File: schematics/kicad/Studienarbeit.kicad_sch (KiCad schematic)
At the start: 65 parts, among them J1 Barrel_Jack_Switch, U1 ESP32-WROOM-32E, U2 PCM5102, U3 MCP6001-OT, U4 MCP6001-OT, U5 MCP6001, U6 TPA711, U7 LM2940CT-5.0

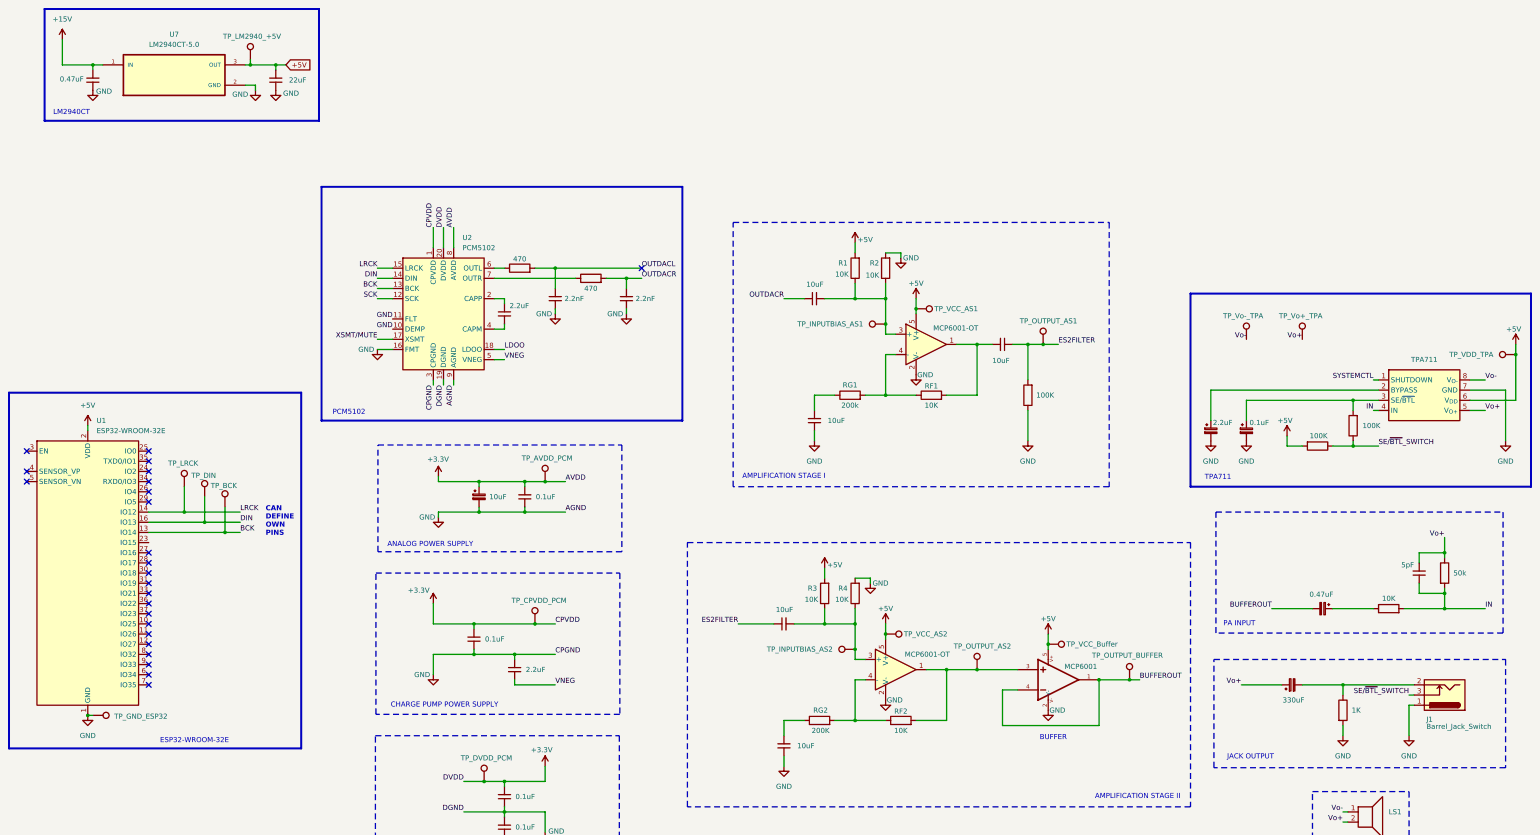
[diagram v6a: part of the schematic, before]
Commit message: Replace ESP32 Schematic with header pins.
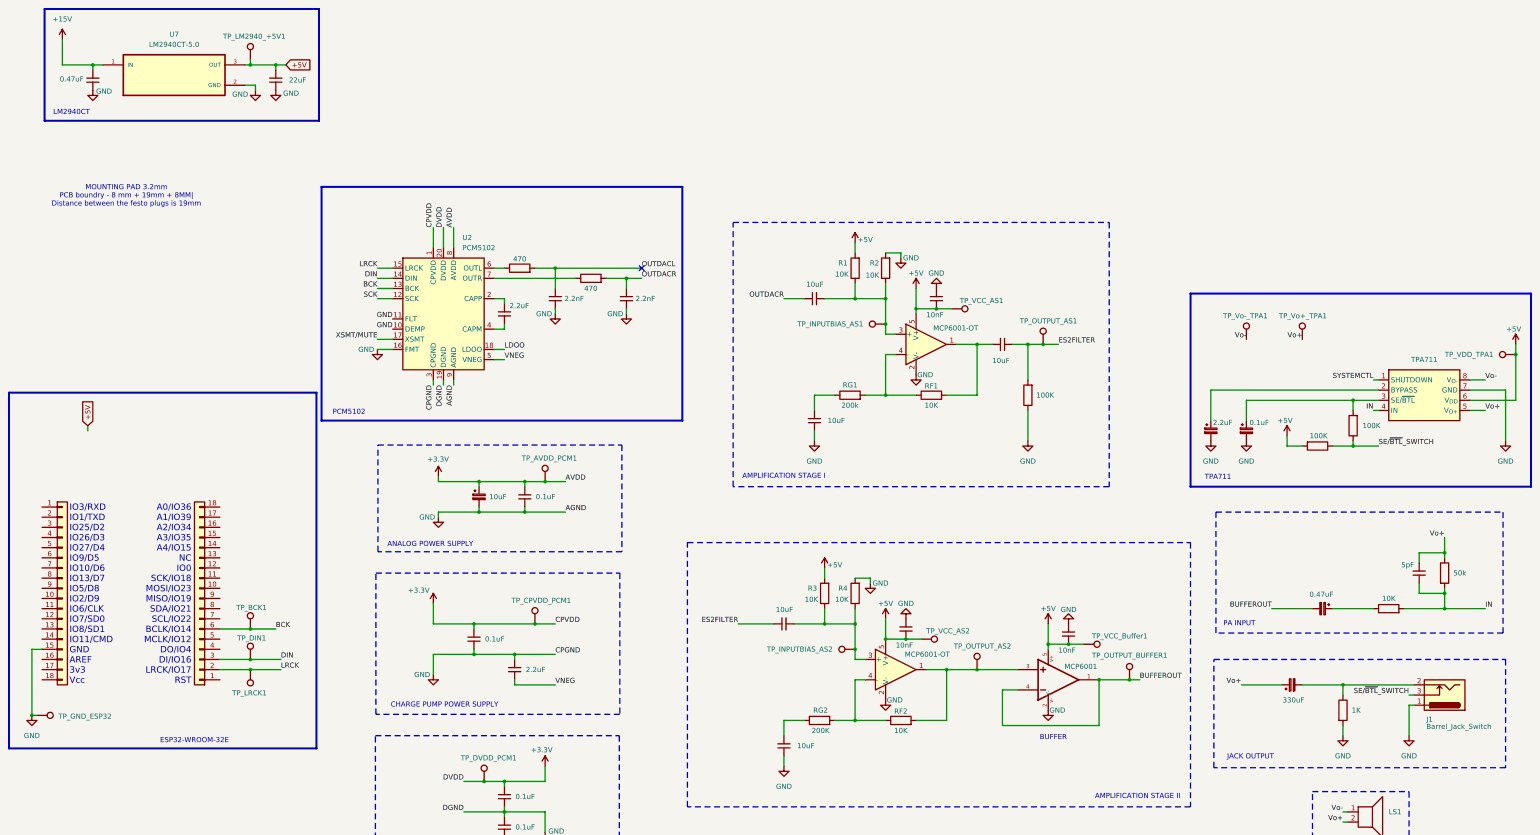
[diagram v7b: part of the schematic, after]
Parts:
- removed U1: ESP32-WROOM-32E, RF_Module:ESP32-WROOM-32E, symbol RF_Module:ESP32-WROOM-32E
- added C_COUPLING_AMPSTAGE2, C_COUPLING_AMPSTAGE3, C_COUPLING_AMPSTAGE4: 10nF, Capacitor_SMD:C_1206_3216Metric_Pad1.33x1.80mm_HandSolder, symbol Device:C_Small
- added J2, J3: Conn_01x18, Connector_PinSocket_2.54mm:PinSocket_1x18_P2.54mm_Vertical, symbol Connector_Generic:Conn_01x18
- TP_AVDD_PCM1: renamed from TP_AVDD_PCM; footprint (none) -> TestPoint:TestPoint_Pad_1.5x1.5mm
- TP_BCK1: renamed from TP_BCK; footprint (none) -> TestPoint:TestPoint_Pad_1.5x1.5mm
- TP_CPVDD_PCM1: renamed from TP_CPVDD_PCM; footprint (none) -> TestPoint:TestPoint_Pad_1.5x1.5mm
- TP_DIN1: renamed from TP_DIN; footprint (none) -> TestPoint:TestPoint_Pad_1.5x1.5mm
- TP_DVDD_PCM1: renamed from TP_DVDD_PCM; footprint (none) -> TestPoint:TestPoint_Pad_1.5x1.5mm
- TP_GND_ESP32, TP_INPUTBIAS_AS1, TP_INPUTBIAS_AS2, TP_OUTPUT_AS1, TP_OUTPUT_AS2, TP_VCC_AS1, TP_VCC_AS2: footprint (none) -> TestPoint:TestPoint_Pad_1.5x1.5mm
- TP_LM2940_+5V1: renamed from TP_LM2940_+5V; footprint (none) -> TestPoint:TestPoint_Pad_1.5x1.5mm
- TP_LRCK1: renamed from TP_LRCK; footprint (none) -> TestPoint:TestPoint_Pad_1.5x1.5mm
- TP_OUTPUT_BUFFER1: renamed from TP_OUTPUT_BUFFER; footprint (none) -> TestPoint:TestPoint_Pad_1.5x1.5mm
- TP_VCC_Buffer1: renamed from TP_VCC_Buffer; footprint (none) -> TestPoint:TestPoint_Pad_1.5x1.5mm
- TP_VDD_TPA1: renamed from TP_VDD_TPA; footprint (none) -> TestPoint:TestPoint_Pad_1.5x1.5mm
- TP_Vo+_TPA1: renamed from TP_Vo+_TPA; footprint (none) -> TestPoint:TestPoint_Pad_1.5x1.5mm
- TP_Vo-_TPA1: renamed from TP_Vo-_TPA; footprint (none) -> TestPoint:TestPoint_Pad_1.5x1.5mm
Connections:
- net +5V: now also C_COUPLING_AMPSTAGE2.2, C_COUPLING_AMPSTAGE3.2, C_COUPLING_AMPSTAGE4.2
- net BCK: now also J3.6 (Pin_6)
- net DIN: now also J3.3 (Pin_3)
- net GND: now also C_COUPLING_AMPSTAGE2.1, C_COUPLING_AMPSTAGE3.1, C_COUPLING_AMPSTAGE4.1, J2.15 (Pin_15)
- net LRCK: now also J3.2 (Pin_2)
- no-connect marks 24 -> 1
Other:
- note added: "A0/IO36 A1/IO39 A2/IO34 A3/IO35 A4/IO15 NC IO0 SCK/IO18 MOSI/IO23 MISO/IO19 SDA/IO21 SCL/IO22 BCLK/IO14 MCLK/IO12 DO/IO4 DI/IO16 LRCK/IO17 RST"
- note added: "IO3/RXD IO1/TXD IO25/D2 IO26/D3 IO27/D4 IO9/D5 IO10/D6 IO13/D7 IO5/D8 IO2/D9 IO6/CLK IO7/SD0 IO8/SD1 IO11/CMD GND AREF 3v3 Vcc"
- note added: "MOUNTING PAD 3.2mm PCB boundry - 8 mm + 19mm + 8MM| Distance between the festo plugs is 19mm"
- note removed: "CAN DEFINE OWN PINS"
- moved on the sheet: TP_BCK1, TP_DIN1, TP_GND_ESP32, TP_LRCK1, TP_VCC_AS1, TP_VCC_AS2, TP_VCC_Buffer1

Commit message: Updated schematic.
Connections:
- net +5V: now also J2.18 (Pin_18)
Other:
- moved on the sheet: TP_BCK1, TP_DIN1, TP_GND_ESP32, TP_LRCK1
